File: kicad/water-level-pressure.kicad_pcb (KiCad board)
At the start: 2 copper layers, 93.3 x 60.1 mm, 38 parts, among them J1 Conn_01x03, J2 Conn_01x02, J3 Conn_01x02, T1 TestPoint, T10 TestPoint, T11 TestPoint, T12 TestPoint, T13 TestPoint, T14 TestPoint, T15 TestPoint, T16 TestPoint, T17 TestPoint, T18 TestPoint, T19 TestPoint, T2 TestPoint, T20 TestPoint, T21 TestPoint, T22 TestPoint, T23 TestPoint, T24 TestPoint, T25 TestPoint, T26 TestPoint, T27 TestPoint, T28 TestPoint, T29 TestPoint, T3 TestPoint, T30 TestPoint, T4 TestPoint, T5 TestPoint, T6 TestPoint, T7 TestPoint, T8 TestPoint, T9 TestPoint

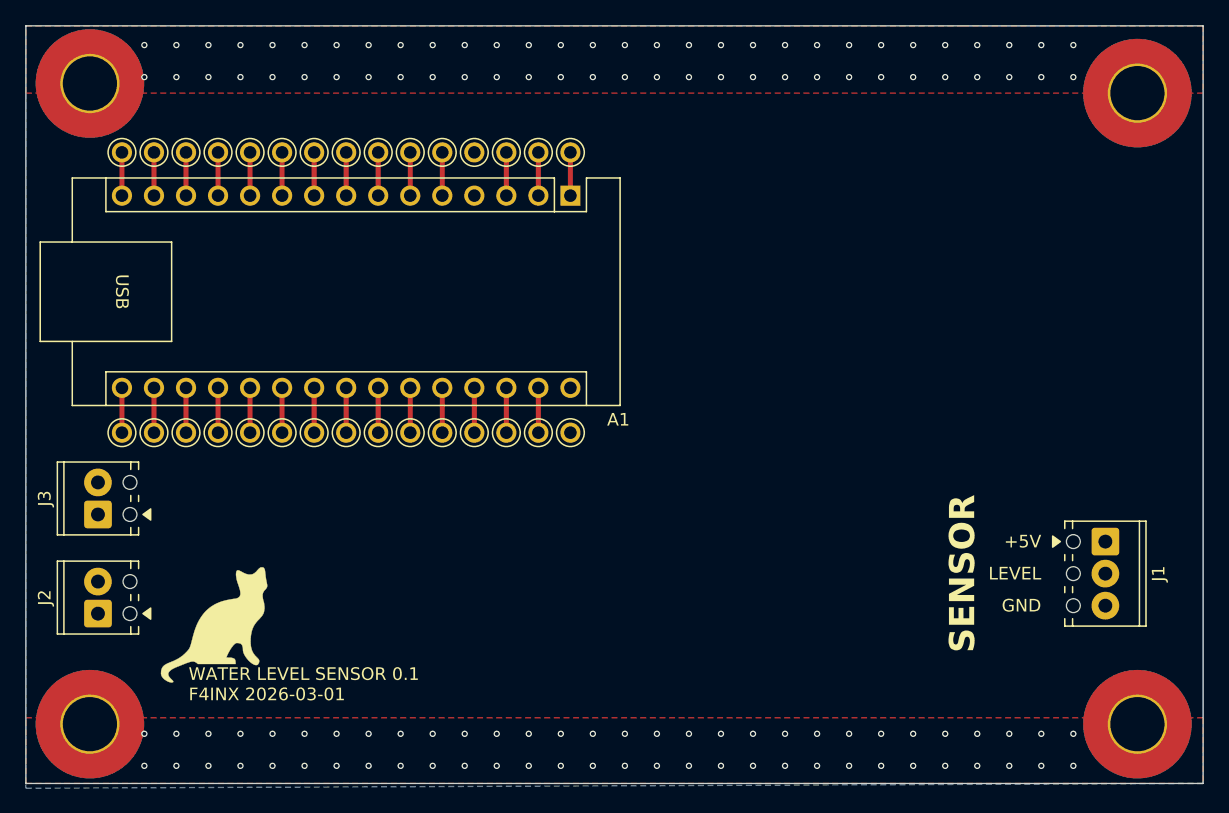
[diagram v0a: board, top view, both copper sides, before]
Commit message: Add 9V battery holder.
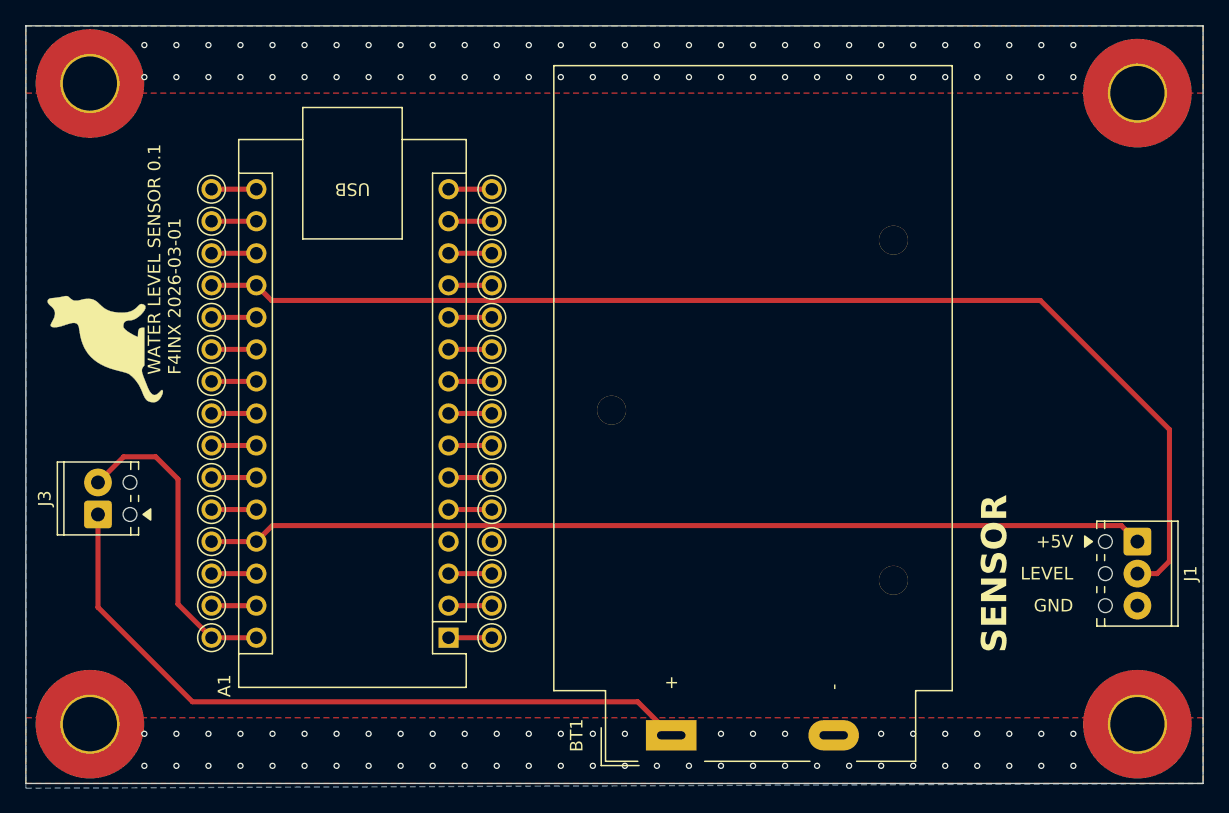
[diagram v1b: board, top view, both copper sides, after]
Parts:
- removed J2: Conn_01x02, TerminalBlock_Phoenix:TerminalBlock_Phoenix_MPT-0,5-2-2.54_1x02_P2.54mm_Horizontal
- added BT1: Battery_Cell, Battery:BatteryHolder_MPD_BA9VPC_1xPP3, F.Cu at (168.0, 138.0)
- moved T1 39.0 mm to (153.8, 130.3), turned to -90 degrees
- moved A1 36.4 mm to (150.4, 130.3), turned to 180 degrees
- moved T2 36.1 mm to (153.8, 127.8), turned to -90 degrees
- moved T3 33.4 mm to (153.8, 125.2), turned to -90 degrees
- moved T30 32.8 mm to (131.6, 130.3), turned to -90 degrees
- moved T4 30.9 mm to (153.8, 122.7), turned to -90 degrees
- moved T15 29.5 mm to (153.8, 94.7), turned to -90 degrees
- moved T29 29.3 mm to (131.6, 127.8), turned to -90 degrees
- moved T5 28.6 mm to (153.8, 120.1), turned to -90 degrees
- moved T14 27.3 mm to (153.8, 97.3), turned to -90 degrees
- moved T6 26.6 mm to (153.8, 117.6), turned to -90 degrees
- moved T28 25.9 mm to (131.6, 125.2), turned to -90 degrees
- moved T13 25.5 mm to (153.8, 99.8), turned to -90 degrees
- moved T7 24.9 mm to (153.8, 115.1), turned to -90 degrees
- moved T12 24.1 mm to (153.8, 102.4), turned to -90 degrees
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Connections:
- net /SCL renamed Net-(A1-SCL/A5)
- net /SDA renamed Net-(A1-SDA/A4)
- net /US_RX renamed Net-(A1-A2)
- net /US_TX_B renamed Net-(A1-A1)
- A1 pad 19: /US_TX_A -> /LEVEL
- J3 pad 2: unconnected-(J3-Pin_2-Pad2) -> /VIN
- T19 pad 1: /US_TX_A -> /LEVEL
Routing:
- net /LEVEL: track 0.00 -> 94.1 mm
- net +5V: track 3.56 -> 74.5 mm
- net /VBAT: track 0.00 -> 57.0 mm
- net /VIN: track 0.00 -> 25.2 mm
- net /US_TX_A: track 3.56 -> 0.00 mm
- net GND: vias 120 -> 116
